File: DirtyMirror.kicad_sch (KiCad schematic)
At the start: 53 parts, among them J101 PWR, SW101 SW_SPDT, U101 TL074, U102 TL074, U103 TL072

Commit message: footprints & layout
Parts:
- R102: value 1k -> 10k
- RV101, RV102: footprint (none) -> Potentiometer_THT:Potentiometer_Alpha_RV16AF_42_Single_Long
- RV103: footprint (none) -> Potentiometer_THT:Potentiometer_Alpha_RV16A01F_41_Dual_Long
- RV104, RV105: footprint 10kB -> Potentiometer_THT:Potentiometer_Alpha_RV16AF_42_Single_Long
- SW101: footprint (none) -> Connector_PinSocket_2.54mm:PinSocket_1x03_P2.54mm_Vertical
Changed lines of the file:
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@@
 			)
 		)
-		(property "Footprint" ""
+		(property "Footprint" "Potentiometer_THT:Potentiometer_Alpha_RV16A01F_41_Dual_Long"
 			(at 220.218 93.472 0)
 			(effects
@@
 			)
 		)
-		(property "Footprint" "10kB"
+		(property "Footprint" "Potentiometer_THT:Potentiometer_Alpha_RV16AF_42_Single_Long"
 			(at 323.85 69.088 0)
 			(effects
@@
 			)
 		)
-		(property "Footprint" "10kB"
+		(property "Footprint" "Potentiometer_THT:Potentiometer_Alpha_RV16AF_42_Single_Long"
 			(at 346.964 81.534 0)
 			(effects
@@
 		(fields_autoplaced yes)
 		(property "Reference" "R102"
-			(at 50.546 193.2939 0)
+			(at 50.8 193.2939 0)
 			(effects
 				(font
@@
 			)
 		)
-		(property "Value" "1k"
-			(at 50.546 195.8339 0)
+		(property "Value" "10k"
+			(at 50.8 195.8339 0)
 			(effects
 				(font
@@
 			)
 		)
-		(property "Footprint" ""
+		(property "Footprint" "Potentiometer_THT:Potentiometer_Alpha_RV16AF_42_Single_Long"
 			(at 86.36 192.024 0)
 			(effects
@@
 			)
 		)
-		(property "Footprint" ""
+		(property "Footprint" "Potentiometer_THT:Potentiometer_Alpha_RV16AF_42_Single_Long"
 			(at 65.532 87.63 0)
 			(effects
@@
 			)
 		)
-		(property "Footprint" ""
+		(property "Footprint" "Connector_PinSocket_2.54mm:PinSocket_1x03_P2.54mm_Vertical"
 			(at 339.852 71.628 0)
 			(effects
@@
 			)
 		)
-		(property "Footprint" ""
+		(property "Footprint" "Potentiometer_THT:Potentiometer_Alpha_RV16A01F_41_Dual_Long"
 			(at 220.472 53.34 0)
 			(effects

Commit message: sallen-key input stage
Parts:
- removed R122: 47k, Resistor_SMD:R_0805_2012Metric, symbol Device:R_US
- removed R123: 100k, Resistor_SMD:R_0805_2012Metric, symbol Device:R_US
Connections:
- net Bias: no longer U103.5 (+)
- net FxFull: now also R121.2, U101.14; no longer U103.7
- net Gtr_Gain: no longer R108.2, R111.1, R114.1, U101.14
- net at U103.1: now also R108.2; no longer R121.2
- net at R120.2, R121.1, RV103.1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: now also U101.13 (-); no longer U103.2 (-)
- net at R109.2, RV102.1: now also U103.2 (-); no longer U101.13 (-)
- new net: R111.1, R114.1
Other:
- note added: "Header & LED"
- note added: "Reference Voltages"
- moved on the sheet: C101, C102, C103, C104, C105, C106, C107, C108, C110, D101, D102, D103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

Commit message: prettified schematic
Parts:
- added C109, C111: 10n, symbol Device:C
- added R122: 10k, symbol Device:R_US
- added R123: 18k, symbol Device:R_US
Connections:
- net Bias: now also C109.2
- net at U103.5 (+): now also C109.1, R123.2
- net Gtr_gain: now reaches U103.6 (-)
- net Gtr_gain: now also R111.1, R114.1, U103.7, C111.2
- net at R108.2, U103.1: now also R122.1
- new net: C111.1, R122.2, R123.1
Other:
- note added: "Input Gain Stage"
- note added: "Precision Rectifiers"
- note added: "Summing Amp & Depth Control"
- note added: "Tone Network & Volume Control"
- note added: "Volume"
- moved on the sheet: C104, C105, C106, C107, C108, R124, R125, R126, R127, R128, RV104, RV105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

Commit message: routed & DRC passing
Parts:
- added J102: ScopeGroundLoop, Connector:THT_GND_WIRE, symbol Connector:ScopeGroundLoop
- added TP101: In, TestPoint:TestPoint_THTPad_D2.0mm_Drill1.0mm_VAL, symbol Connector:TestPoint
- added TP102: Out, TestPoint:TestPoint_THTPad_D2.0mm_Drill1.0mm_VAL, symbol Connector:TestPoint
- added TP103: LT, TestPoint:TestPoint_THTPad_D2.0mm_Drill1.0mm_VAL, symbol Connector:TestPoint
- added TP104: HT, TestPoint:TestPoint_THTPad_D2.0mm_Drill1.0mm_VAL, symbol Connector:TestPoint
- added TP105: Bias, TestPoint:TestPoint_THTPad_D2.0mm_Drill1.0mm_VAL, symbol Connector:TestPoint
- added TP106: LR, TestPoint:TestPoint_THTPad_D2.0mm_Drill1.0mm_VAL, symbol Connector:TestPoint
- added TP107: HR, TestPoint:TestPoint_THTPad_D2.0mm_Drill1.0mm_VAL, symbol Connector:TestPoint
- added TP108: FF, TestPoint:TestPoint_THTPad_D2.0mm_Drill1.0mm_VAL, symbol Connector:TestPoint
- added TP109: GG, TestPoint:TestPoint_THTPad_D2.0mm_Drill1.0mm_VAL, symbol Connector:TestPoint
- C109: value 10n -> 4n7; footprint (none) -> Capacitor_SMD:C_0805_2012Metric
- C111: value 10n -> 2n2; footprint (none) -> Capacitor_SMD:C_0805_2012Metric
- R106, R107: value 47k -> 22k
- R122: value 10k -> 47k; footprint (none) -> Resistor_SMD:R_0805_2012Metric
- R123: value 18k -> 47k; footprint (none) -> Resistor_SMD:R_0805_2012Metric
- U101, U102: footprint Package_SO:SOIC-14_3.9x8.7mm_P1.27mm -> Package_DIP:DIP-14_W7.62mm
- U103: footprint Package_SO:SOIC-8_3.9x4.9mm_P1.27mm -> Package_DIP:DIP-8_W7.62mm
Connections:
- net Gtr_Gain is gone; now on net Gtr_gain: R120.1
- net Bias: now also TP105.1
- net FX_IN: now also TP101.1
- net FX_OUT: now also TP102.1
- net FxFull: now also TP108.1
- net GND: now also J102.1
- net Gtr_gain: now also TP109.1
- net HiRect: now also TP107.1
- net HiThresh: now also TP104.1
- net LoRect: now also TP106.1
- net LoThresh: now also TP103.1
- net at RV103.6: now also R120.2, R121.1, RV103.3, U101.13 (-); no longer R119.2
- net at R118.2: now also RV103.1, RV103.2; no longer RV103.3
- new net: R119.2, RV103.4, RV103.5
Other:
- moved on the sheet: RV103A, RV103B

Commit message: rev2 simulation
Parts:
- C103, C106: value 1u -> 2u2
- C111: value 2n2 -> 2n7
- R102: value 10k -> 6k8
- R108: value 3k3 -> 100k
- R109: value 3k3 -> 12k
- R120: value 47k -> 33k
- R121: value 47k -> 220k
- RV101: value 10k -> 10kB
- RV102: value 10kB -> 100kB
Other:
- moved on the sheet: C103, C104, C105, C106, C107, C108, C109, C111, D101, D102, D103, D104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

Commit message: rev2 rough routing
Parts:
- removed C105: 100n, Capacitor_SMD:C_0805_2012Metric, symbol Device:C
- removed RV103: 100kB, Potentiometer_THT:Potentiometer_Alpha_RV16A01F_41_Dual_Long, symbol Device:R_Potentiometer_Dual_Separate
- removed U103: TL072, Package_DIP:DIP-8_W7.62mm, symbol Amplifier_Operational:TL072
- added R130: 33k, Resistor_SMD:R_0805_2012Metric, symbol Device:R_US
- added R131: 10k, Resistor_SMD:R_0805_2012Metric, symbol Device:R_US
- added R132, R134: 4k7, Resistor_SMD:R_0805_2012Metric, symbol Device:R_US
- added R133, R135: 47k, Resistor_SMD:R_0805_2012Metric, symbol Device:R_US
- added R136: 100k, Resistor_SMD:R_0805_2012Metric, symbol Device:R_US
- added RV103: 10kB, Potentiometer_THT:Potentiometer_Alpha_RV16AF_42_Single_Long, symbol Device:R_Potentiometer_US
- added TP110: CLIP, TestPoint:TestPoint_THTPad_D2.0mm_Drill1.0mm_VAL, symbol Connector:TestPoint
- added TP111: FOLD, TestPoint:TestPoint_THTPad_D2.0mm_Drill1.0mm_VAL, symbol Connector:TestPoint
- R101: value 100k -> 56k
- R102: value 6k8 -> 1k
- R103: value 100k -> 68k
- R106: value 22k -> 56k
- R107: value 22k -> 68k
- R108: value 100k -> 680k
- R109: value 12k -> 100k
- R119: value 47k -> 68k
- R120: value 33k -> 47k
- R121: value 220k -> 68k
- R129: value 3k3 -> 4k7
- RV102: value 100kB -> 10k
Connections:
- net +9V: now also R106.1
- net Bias: now also R102.2, U101.3 (+), U101.6 (-), U101.7, U102.12 (+), U102.5 (+), R131.2, RV103.2; no longer R112.1, R116.1, U101.1, U101.10 (+), U101.2 (-)
- net FxFull: now also U101.1, R136.2; no longer R121.2, U101.14
- net GND: now also R107.2
- net Gtr_gain: now also R112.1, R119.1, U101.8, R130.2; no longer R120.1
- net HiRect: now also D102.2 (A), R110.2, R113.1; no longer R113.2, U102.7
- net HiThresh: now also R101.2, R103.1; no longer RV101.1, U101.6 (-), U101.7
- net LoRect: now also D104.1 (K), R115.2, R116.1, R120.1; no longer R117.2, R119.1, U102.14
- net LoThresh: now also R107.1, RV101.2, RV101.3; no longer R107.2, U101.8
- net at C109.1, R123.2: now also U101.10 (+)
- net at R116.2, R117.1: now also R112.2, R113.2, U102.6 (-); no longer U102.13 (-)
- net at R120.2, R121.1: now also R118.2, R119.2, U102.13 (-); no longer U101.13 (-)
- net at R108.2: now also RV102.3, U101.14; no longer R122.1
- net at R109.2: now also R108.1, U101.13 (-); no longer RV102.1
- net at C102.1, R104.2, R105.1: now also U101.5 (+); no longer U101.3 (+)
- new net: R134.2, R135.1, RV103.1
- new net: R132.2, R133.1, RV103.3
- new net: R133.2, R135.2, R136.1, U101.2 (-)
- new net: R102.1, RV102.1
- new net: R122.1, RV102.2
- new net: R130.1, R131.1, U101.9 (-)
- new net: R106.2, RV101.1
- new net Clip: R117.2, R132.1, TP110.1, U102.7
- new net Fold: R121.2, R134.1, TP111.1, U102.14
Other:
- note added: "Mix"
- note added: "Output Mixer"
- note removed: "Depth"
- note removed: "Summing Amp & Depth Control"
- moved on the sheet: C103, C104, C106, C107, C108, C109, C111, D101, D102, D103, D104, R108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

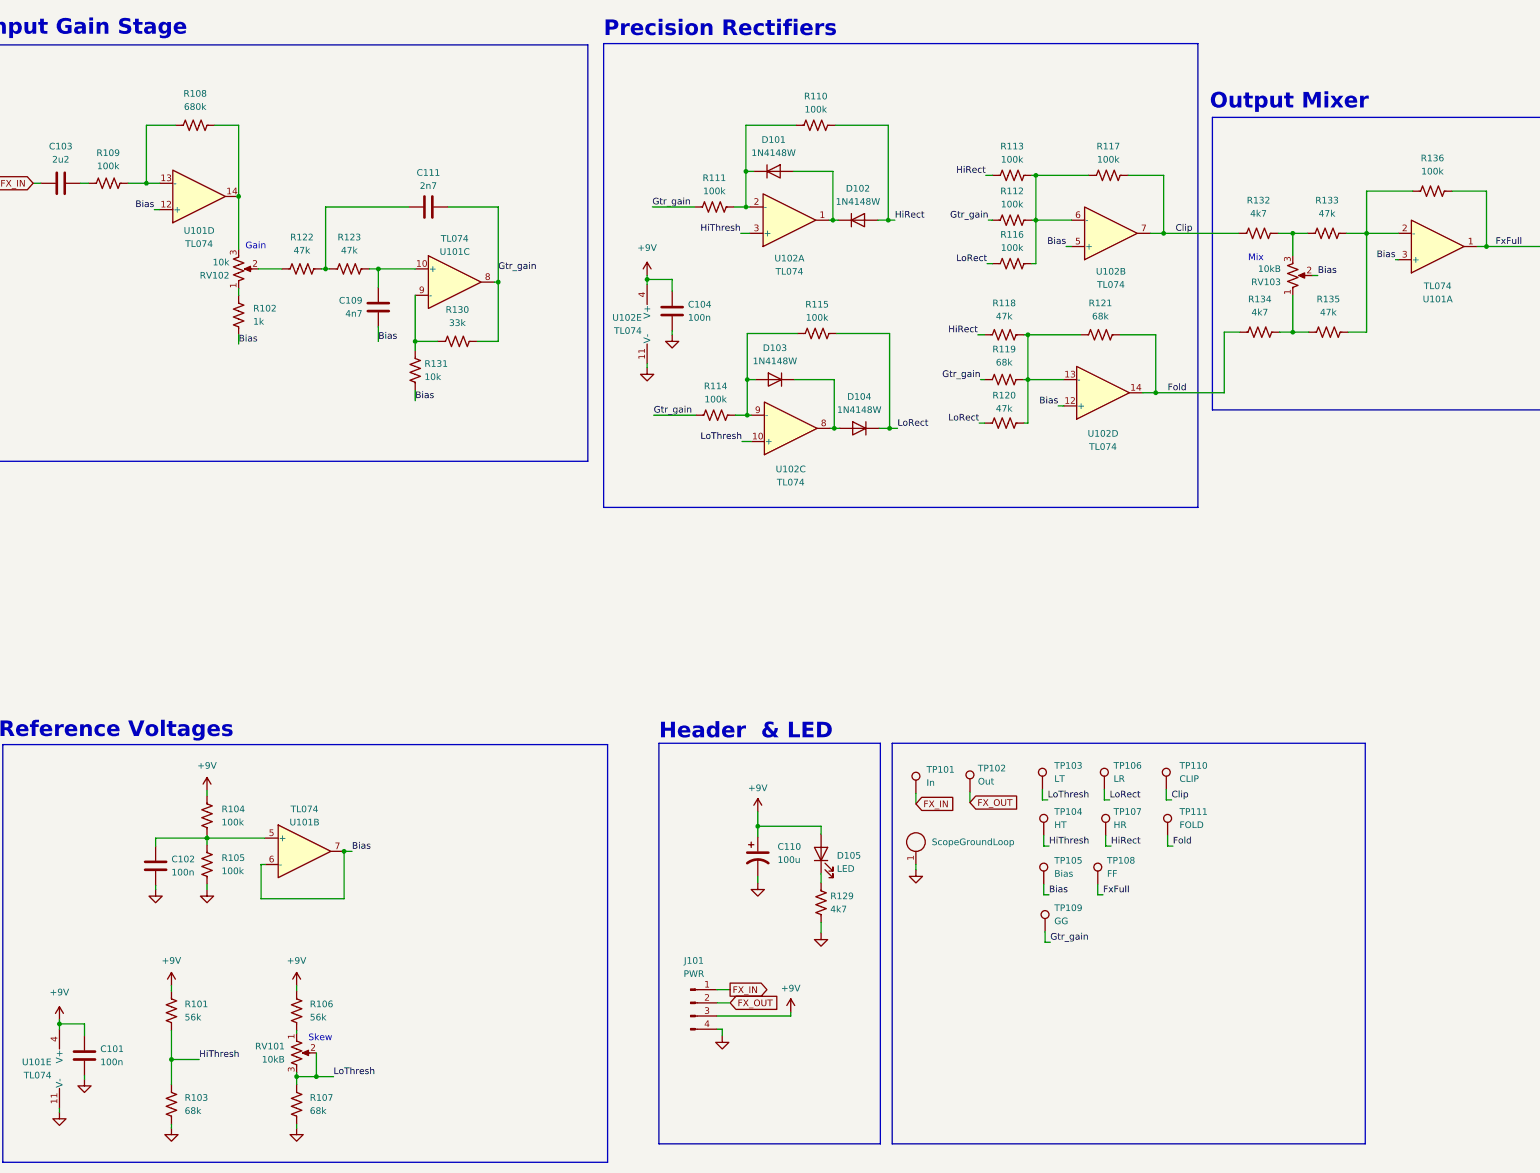
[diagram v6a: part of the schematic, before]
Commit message: pedal working, tweaked a few component values
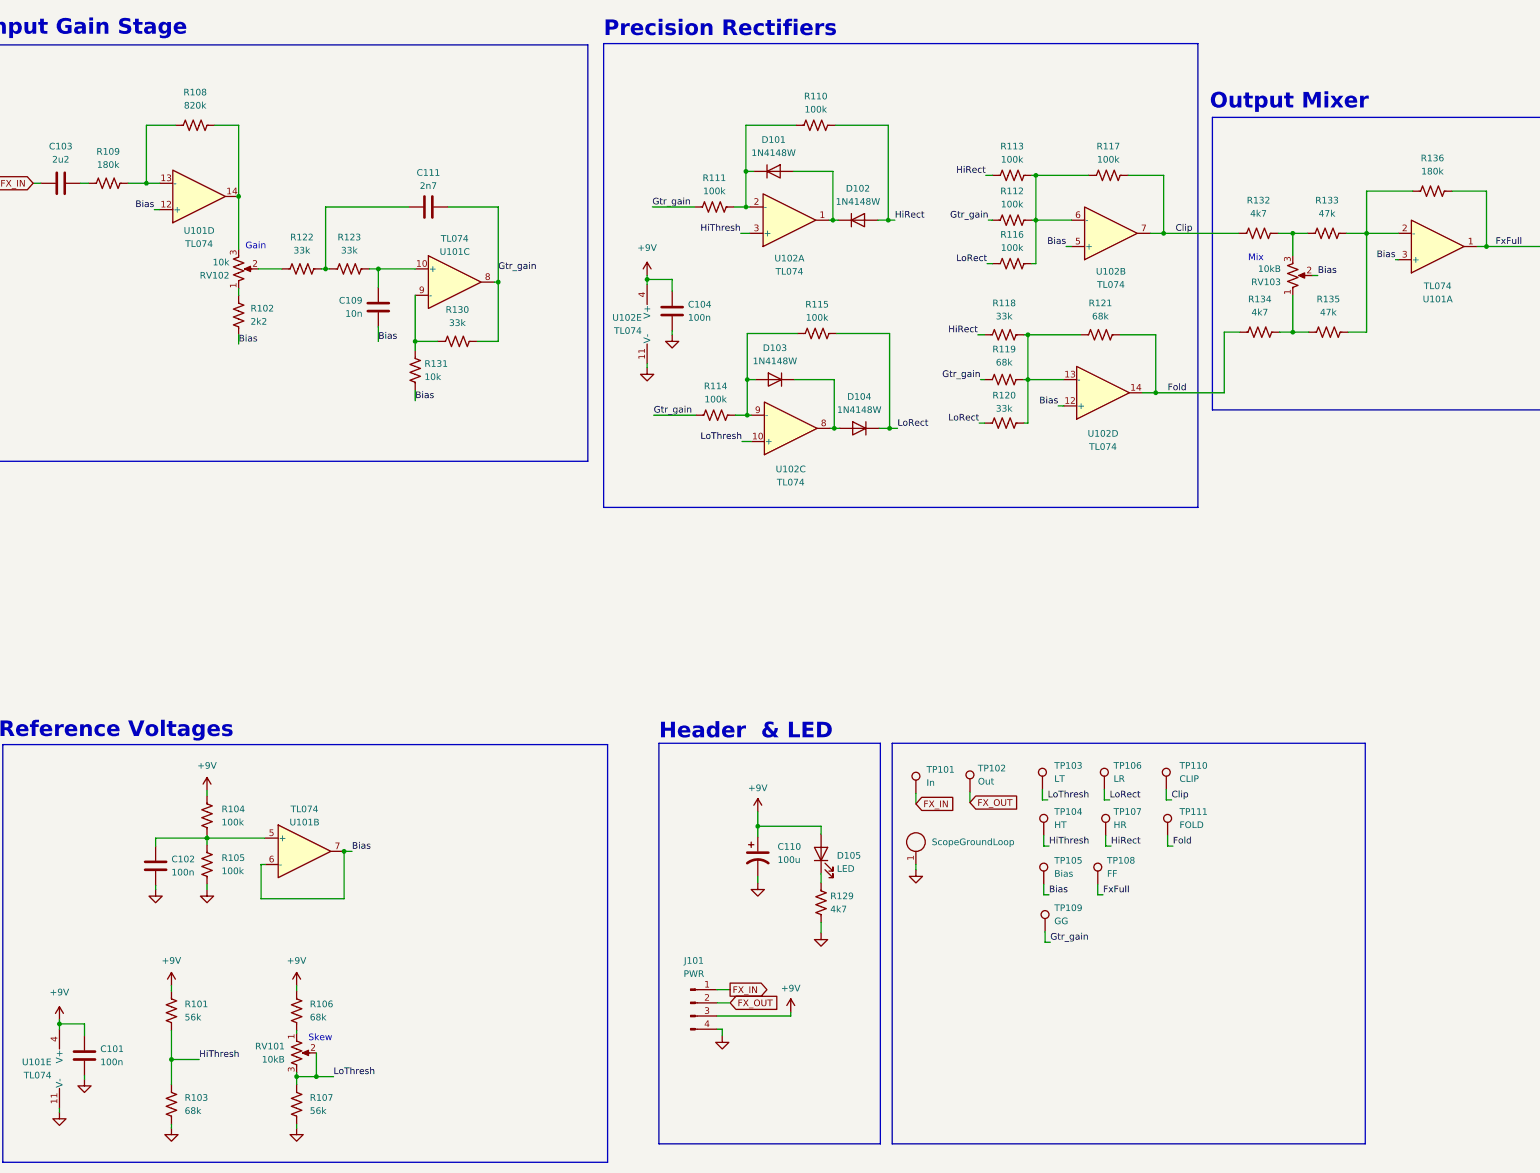
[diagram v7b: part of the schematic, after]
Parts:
- C109: value 4n7 -> 10n
- R102: value 1k -> 2k2
- R106: value 56k -> 68k
- R107: value 68k -> 56k
- R108: value 680k -> 820k
- R109, R136: value 100k -> 180k
- R118, R120, R122, R123: value 47k -> 33k
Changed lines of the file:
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@@
 		(fields_autoplaced yes)
 		(property "Reference" "R102"
-			(at 65.278 82.2959 0)
+			(at 64.77 82.2959 0)
 			(effects
 				(font
@@
 			)
 		)
-		(property "Value" "1k"
-			(at 65.278 84.8359 0)
+		(property "Value" "2k2"
+			(at 64.77 84.8359 0)
 			(effects
 				(font
@@
 			)
 		)
-		(property "Value" "47k"
+		(property "Value" "33k"
 			(at 74.676 71.12 90)
 			(effects
@@
 		(fields_autoplaced yes)
 		(property "Reference" "R109"
-			(at 37.338 52.324 90)
+			(at 37.338 52.07 90)
 			(effects
 				(font
@@
 			)
 		)
-		(property "Value" "100k"
-			(at 37.338 54.864 90)
+		(property "Value" "180k"
+			(at 37.338 54.61 90)
 			(effects
 				(font
@@
 			)
 		)
-		(property "Value" "47k"
+		(property "Value" "33k"
 			(at 210.058 101.6 90)
 			(effects
@@
 			)
 		)
-		(property "Value" "68k"
+		(property "Value" "56k"
 			(at 76.2 236.9819 0)
 			(effects
@@
 			)
 		)
-		(property "Value" "56k"
+		(property "Value" "68k"
 			(at 76.2 218.9479 0)
 			(effects
@@
 			)
 		)
-		(property "Value" "47k"
+		(property "Value" "33k"
 			(at 83.82 71.12 90)
 			(effects
@@
 			)
 		)
-		(property "Value" "4n7"
+		(property "Value" "10n"
 			(at 86.36 83.3119 0)
 			(effects
@@
 			)
 		)
-		(property "Value" "47k"
+		(property "Value" "33k"
 			(at 210.058 83.82 90)
 			(effects
@@
 			)
 		)
-		(property "Value" "100k"
+		(property "Value" "180k"
 			(at 292.608 55.88 90)
 			(effects
@@
 		(fields_autoplaced yes)
 		(property "Reference" "R108"
-			(at 54.102 40.894 90)
+			(at 54.102 40.64 90)
 			(effects
 				(font
@@
 			)
 		)
-		(property "Value" "680k"
-			(at 54.102 43.434 90)
+		(property "Value" "820k"
+			(at 54.102 43.18 90)
 			(effects
 				(font
